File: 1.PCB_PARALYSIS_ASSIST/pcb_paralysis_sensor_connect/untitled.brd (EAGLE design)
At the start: 160 x 100 mm, 7 parts

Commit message: small board
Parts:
- added LED1: (no value), led:CHIP-LED0805
- added R3: 1k, adafruit:M0805
- moved R2 21.0 mm to (26.6, 13.3), flipped to the bottom
- moved R1 19.9 mm to (26.6, 8.27), flipped to the bottom, turned to 90 degrees
- moved SOUND_IN 16.0 mm to (10.3, 28.6)
- moved JP2 13.9 mm to (6.32, 12.1), turned to 180 degrees
- moved JP1 11.5 mm to (25.5, 42.8), turned to 90 degrees
- moved MPU6050 9.46 mm to (26.6, 26.0)
- moved SENSOR_CONNECT 3.20 mm to (16.5, 5.73)
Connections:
- removed net N$2: SENSOR_CONNECT.5
- removed net N$3: SENSOR_CONNECT.3
- removed net N$4: SENSOR_CONNECT.1
- removed net N$5: SENSOR_CONNECT.8
- removed net N$6: SENSOR_CONNECT.6
- removed net N$7: SENSOR_CONNECT.4
- removed net N$8: SENSOR_CONNECT.2
- net 5V: now also R3.1, SENSOR_CONNECT.1, SENSOR_CONNECT.4
- net GND: now also LED1.C, SENSOR_CONNECT.3
- net N$1: now also LED1.A, R3.2; no longer SENSOR_CONNECT.7
- net SCL: now also SENSOR_CONNECT.8
- net SDA: now also SENSOR_CONNECT.7
- net SOUND_A0: now also SENSOR_CONNECT.6
- net SOUND_D0: now also SENSOR_CONNECT.2
- net TEMP_DATA: now also SENSOR_CONNECT.5
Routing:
- net 5V: track 0.00 -> 120.4 mm, vias 0 -> 2
- net GND: track 0.00 -> 90.7 mm, vias 0 -> 4
- net TEMP_DATA: track 0.00 -> 58.8 mm
- net SCL: track 0.00 -> 41.8 mm
- net SDA: track 0.00 -> 33.5 mm, vias 0 -> 2
- net SOUND_D0: track 0.00 -> 24.8 mm
- net SOUND_A0: track 0.00 -> 23.1 mm
- net N$1: track 0.00 -> 4.33 mm
- added copper zone on layer 16, net GND
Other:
- board size 160 x 100 mm -> 35.6 x 48.3 mm

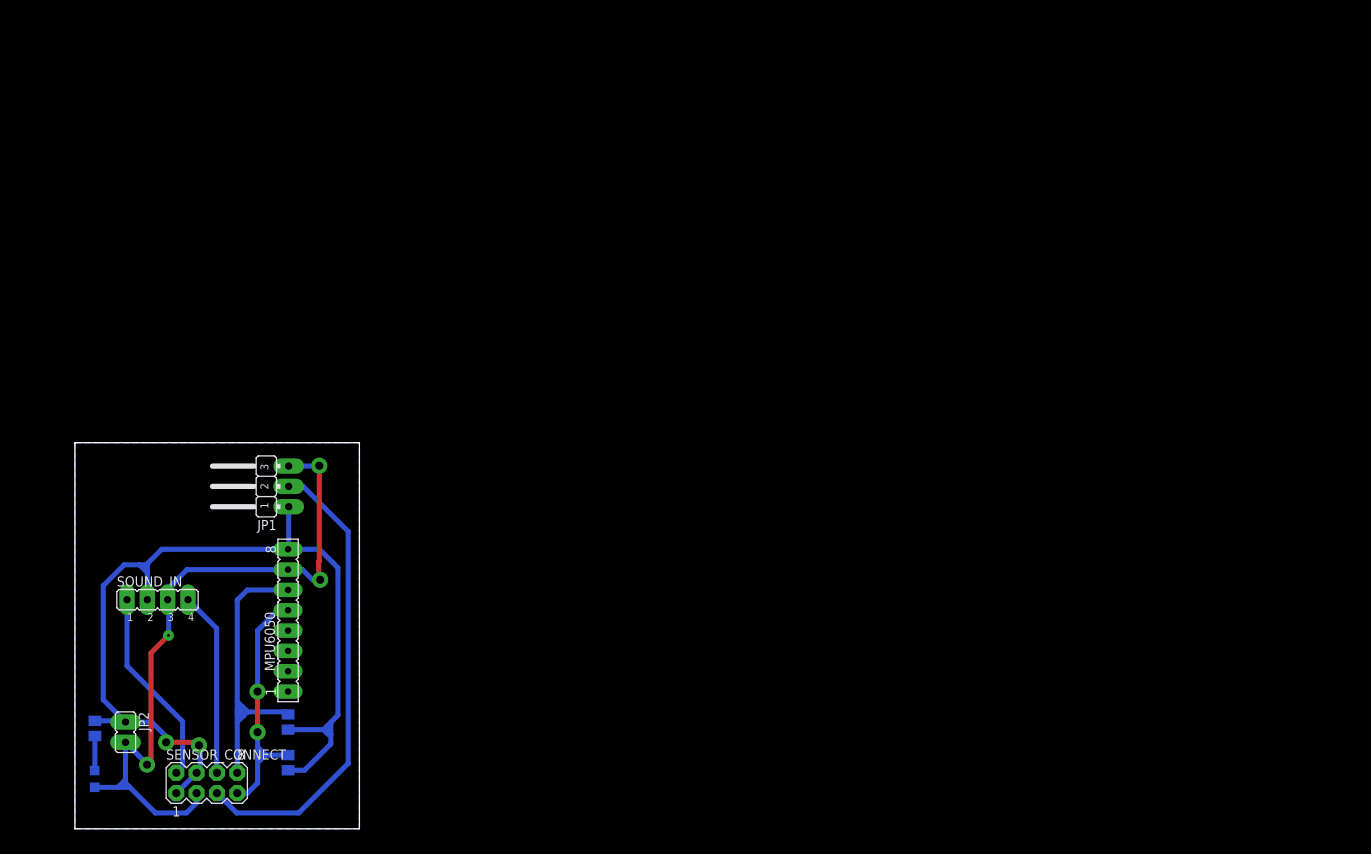
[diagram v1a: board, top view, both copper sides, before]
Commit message: updated version_2 layout
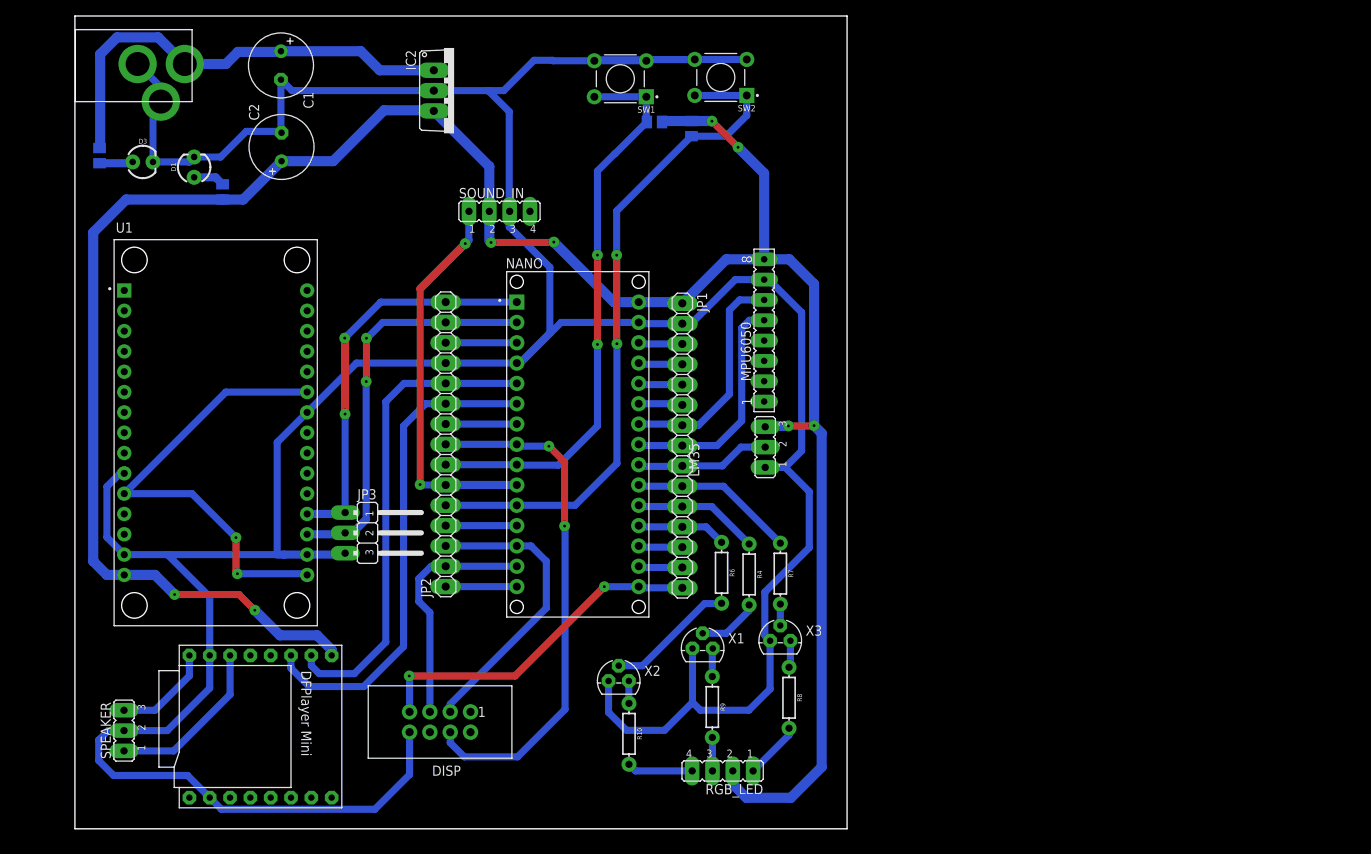
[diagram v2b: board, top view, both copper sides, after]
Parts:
- removed LED1: (no value), led:CHIP-LED0805
- removed SENSOR_CONNECT: (no value), con-lstb:MA04-2
- added C1, C2: (no value), adafruit:E3,5-8
- added D1, D3: (no value), SparkFun-LED:LED_3MM
- added DISP: (no value), Wurth_Elektronik_Electromechanic_Wire_to_Board_Connectors_rev19a:612008235121
- added IC2: 7805TV, linear:TO220V
- added JP3: (no value), jumper:JP2W
- added LM35, SPEAKER: (no value), jumper:JP2
- added NANO: A000005, A000005:MODULE_A000005
- added R10, R4, R6, R7, R8, R9: 330, SparkFun-Resistors:AXIAL-0.3
- added R11: 1k, adafruit:M0805
- added RGB_LED: (no value), jumper:JP4
- added SW1, SW2: 1825910-2, 1825910-2:TE_1825910-2
- added U$1: DFPLAYER, DFPlayer_v1:DFPLAYER
- added U$3: 2.1MMJACKTHM, adafruit:PJ-102A
- added U1: ZC563900, nodemcuZC563900:MODULE_ZC563900
- added X1, X2, X3: (no value), sym:TO92
- JP1: device jumper:JP2W -> adafruit:1X15
- JP2: device jumper:JP1 -> adafruit:1X15
- moved R3 103.1 mm to (72.4, 88.4), turned to 0 degrees
- moved R2 89.7 mm to (77.1, 87.5), turned to 270 degrees
- moved R1 71.8 mm to (18.5, 79.6)
- moved MPU6050 69.7 mm to (86.2, 62.3)
- moved SOUND_IN 64.7 mm to (53.1, 77.2)
- moved JP2 53.8 mm to (46.3, 48.1), turned to 90 degrees
- moved JP1 50.7 mm to (75.9, 47.9), turned to 270 degrees
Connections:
- removed net TEMP_DATA: JP1.2, SENSOR_CONNECT.5
- new net 3V3: U1.11, U1.16, U1.25
- new net 5V0: JP1.4, NANO.27
- new net 9_IN: C1.+, IC2.1, R11.1, U$3.TIP
- new net A0: JP1.12, NANO.19, R6.P$1
- new net A1: JP1.11, NANO.20, R4.P$1
- new net A2: JP1.10, NANO.21, R7.P$1
- new net A6: JP1.6, NANO.25
- new net A7: JP1.5, NANO.26
- new net AD0: MPU6050.2
- new net AREF: JP1.13, NANO.18
- new net BACK: JP2.5, NANO.11, R2.2, SW2.1, SW2.2
- new net BASE_BLUE: R6.P$2, X2.2
- new net BASE_GREEN: R4.P$2, X1.2
- new net BASE_RED: R7.P$2, X3.2
- new net BLUE: R10.P$2, RGB_LED.4
- new net COLLECTOR_BLUE: R10.P$1, X2.1
- new net COLLECTOR_GREEN: R9.P$1, X1.1
- new net COLLECTOR_RED: R8.P$1, X3.1
- new net CS_DISP: DISP.3, JP2.3, NANO.13
- new net D4: JP2.9, NANO.7
- new net D9: JP2.4, NANO.12
- new net GREEN: R9.P$2, RGB_LED.3
- new net INT: MPU6050.1
- new net MISO: JP2.1, NANO.15
- new net MOSI: DISP.5, JP2.2, NANO.14
- new net N$13: U$1.DAC_R
- new net N$14: U$1.DAC_L
- new net N$18: U$1.BUSY
- new net N$19: U$1.USB-
- new net N$2: D3.A, R11.2
- new net N$20: U$1.USB+
- new net N$21: U$1.ADKEY2
- new net N$22: U$1.ADKEY1
- new net N$23: U$1.IO2
- new net N$25: U$1.IO1
- new net N$3: D1.A, R1.2
- new net N$5: DISP.6
- new net N$8: JP1.14, NANO.17
- new net OK: JP2.7, NANO.9, R3.2, SW1.1, SW1.2
- new net RED: R8.P$2, RGB_LED.1
- new net RESET_1: JP2.13, NANO.3
- new net RESET_2: JP1.3, NANO.28
- new net RST: DISP.4, JP2.8, NANO.8
- new net RXNANO: JP2.14, JP3.2, NANO.2, U1.18
- new net RX_DF: JP2.11, NANO.5, U$1.RX
- new net SCK: DISP.7, JP1.15, NANO.16
- new net SPK_1: SPEAKER.1, U$1.SPK1
- new net SPK_2: SPEAKER.3, U$1.SPK2
- new net TEMP: JP1.9, LM35.2, NANO.22
- new net TXNANO: JP2.15, JP3.1, NANO.1, U1.19
- new net TX_DF: JP2.10, NANO.6, U$1.TX
- new net VCC: DISP.1
- new net XCL: MPU6050.3
- new net XDA: MPU6050.4
- net 5V: now also C2.+, IC2.3, LM35.3, NANO.30, RGB_LED.2, U$1.VCC, U1.15; no longer JP2.1, SENSOR_CONNECT.1, SENSOR_CONNECT.4
- net GND: now also C1.-, C2.-, D1.K, D3.K, DISP.8, IC2.2, JP1.2, JP2.12, JP3.3, LM35.1, NANO.29, NANO.4, SPEAKER.2, SW1.3, SW1.4, SW2.3, SW2.4, U$1.GND_1, U$1.GND_2, U$3.RING, U$3.RING_SW, U1.10, U1.14, U1.17, U1.24, X1.3, X2.3, X3.3; no longer JP1.3, JP2.2, LED1.C, SENSOR_CONNECT.3
- net N$1: now also DISP.2; no longer LED1.A, R3.2
- net SCL: now also JP1.7, NANO.24; no longer R2.2, SENSOR_CONNECT.8
- net SDA: now also JP1.8, NANO.23; no longer R1.2, SENSOR_CONNECT.7
- net SOUND_A0: no longer SENSOR_CONNECT.6
- net SOUND_D0: now also JP2.6, NANO.10; no longer SENSOR_CONNECT.2
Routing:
- net GND: track 90.7 -> 443.9 mm, vias 4 -> 0
- net 5V: track 120.4 -> 300.1 mm, vias 2 -> 8
- net BACK: track 0.00 -> 85.4 mm, vias 0 -> 2
- net OK: track 0.00 -> 71.3 mm, vias 0 -> 2
- net RST: track 0.00 -> 65.6 mm, vias 0 -> 2
- net TX_DF: track 0.00 -> 61.6 mm
- net RX_DF: track 0.00 -> 60.0 mm
- net TEMP_DATA: track 58.8 -> 0.00 mm
- net 3V3: track 0.00 -> 57.8 mm, vias 0 -> 2
- net 9_IN: track 0.00 -> 57.4 mm
- net RXNANO: track 0.00 -> 50.7 mm, vias 0 -> 2
- net TXNANO: track 0.00 -> 50.0 mm, vias 0 -> 2
- net SCK: track 0.00 -> 43.3 mm, vias 0 -> 2
- net CS_DISP: track 0.00 -> 37.2 mm
- net MOSI: track 0.00 -> 30.1 mm
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- removed copper zone on layer 16, net GND
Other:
- board size 35.6 x 48.3 mm -> 96.5 x 101.6 mm
